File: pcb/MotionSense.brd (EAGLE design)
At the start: 59.4 x 59.2 mm, 18 parts

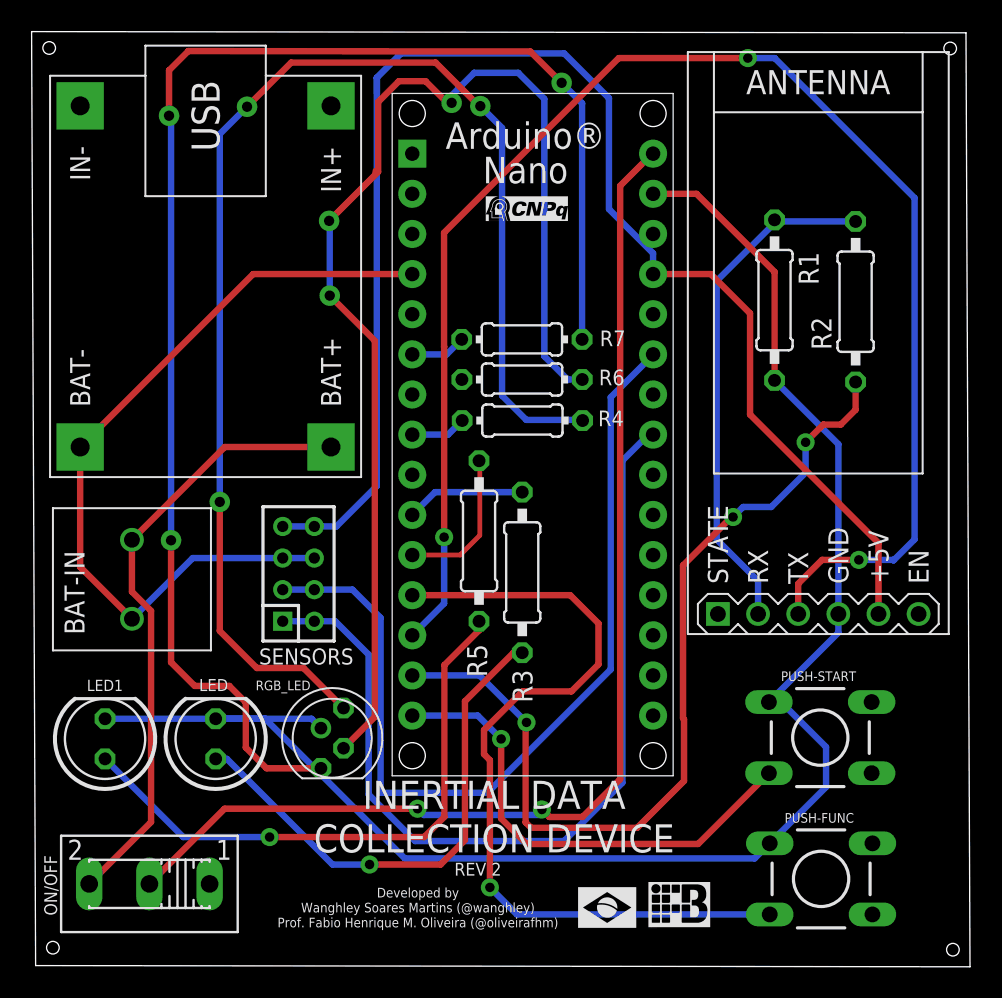
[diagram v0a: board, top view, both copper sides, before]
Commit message: [UPDATE] Wrong ports and errors in design fixing
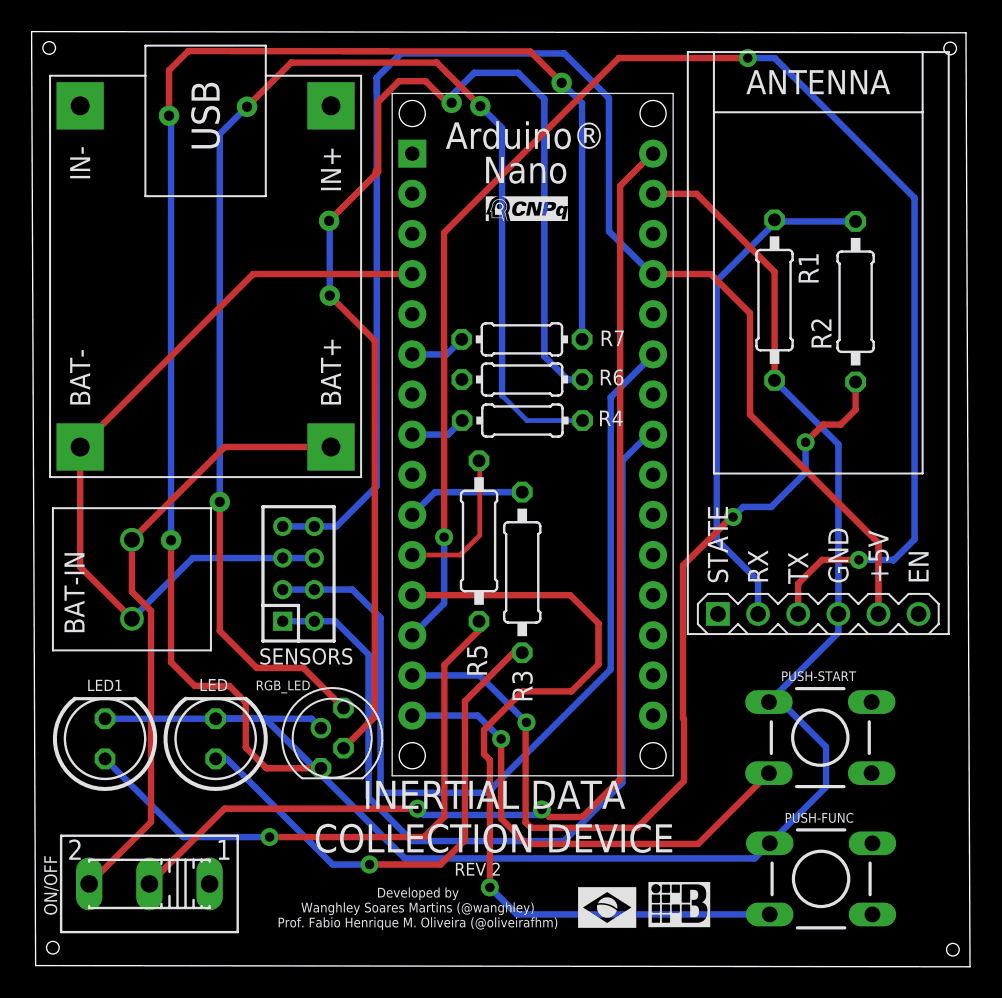
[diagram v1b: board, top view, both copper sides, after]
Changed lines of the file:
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@@
 <wire x1="40.5732" y1="36.9288" x2="41.9001" y2="36.9288" width="0.4064" layer="16"/>
 <wire x1="41.9001" y1="36.9288" x2="44.015659375" y2="34.813240625" width="0.4064" layer="16"/>
-<wire x1="44.015659375" y1="34.813240625" x2="44.015659375" y2="25.958796875" width="0.4064" layer="16"/>
-<wire x1="44.015659375" y1="25.958796875" x2="46.95570625" y2="23.01875" width="0.4064" layer="16"/>
-<wire x1="46.95570625" y1="23.01875" x2="56.379109375" y2="23.01875" width="0.4064" layer="16"/>
+<wire x1="44.015659375" y1="34.813240625" x2="44.015659375" y2="25.765759375" width="0.4064" layer="16"/>
+<wire x1="44.015659375" y1="25.765759375" x2="46.76266875" y2="23.01875" width="0.4064" layer="16"/>
+<wire x1="46.76266875" y1="23.01875" x2="56.379109375" y2="23.01875" width="0.4064" layer="16"/>
 <wire x1="61.716921875" y1="48.7400625" x2="60.0684625" y2="47.091603125" width="0.4064" layer="16"/>
 <wire x1="61.716921875" y1="48.7400625" x2="62.0115625" y2="48.7400625" width="0.4064" layer="16"/>
@@
 <wire x1="46.07051875" y1="72.86751875" x2="56.38038125" y2="72.86751875" width="0.4064" layer="16"/>
 <wire x1="56.38038125" y1="72.86751875" x2="59.2201" y2="70.0278" width="0.4064" layer="16"/>
-<wire x1="59.2201" y1="70.0278" x2="59.2201" y2="63.00588125" width="0.4064" layer="16"/>
-<wire x1="62.0115625" y1="58.9000625" x2="62.0115625" y2="60.21441875" width="0.4064" layer="16"/>
-<wire x1="62.0115625" y1="60.21441875" x2="59.2201" y2="63.00588125" width="0.4064" layer="16"/>
+<wire x1="59.2201" y1="70.0278" x2="59.2201" y2="61.603803125" width="0.4064" layer="16"/>
+<wire x1="62.0115625" y1="58.9000625" x2="61.923840625" y2="58.9000625" width="0.4064" layer="16"/>
+<wire x1="61.923840625" y1="58.9000625" x2="59.2201" y2="61.603803125" width="0.4064" layer="16"/>
 <wire x1="38.5732" y1="42.9288" x2="40.5732" y2="42.9288" width="0.4064" layer="16"/>
 <wire x1="76.2762" y1="37.3888" x2="76.2762" y2="41.8846" width="0.4064" layer="1"/>
@@
 <wire x1="57.4929" y1="49.8221" x2="57.4929" y2="49.819559375" width="0.4064" layer="16"/>
 <wire x1="36.316921875" y1="69.489321875" x2="39.11091875" y2="72.28331875" width="0.4064" layer="1"/>
-<wire x1="39.11091875" y1="72.28331875" x2="48.249840625" y2="72.28331875" width="0.4064" layer="1"/>
-<wire x1="48.249840625" y1="72.28331875" x2="50.8609625" y2="69.672196875" width="0.4064" layer="1"/>
-<wire x1="50.9371625" y1="69.672196875" x2="50.8609625" y2="69.672196875" width="0.4064" layer="1"/>
-<wire x1="50.9371625" y1="69.672196875" x2="51.0794" y2="69.529959375" width="0.4064" layer="1"/>
+<wire x1="39.11091875" y1="72.28331875" x2="48.326040625" y2="72.28331875" width="0.4064" layer="1"/>
+<wire x1="48.326040625" y1="72.28331875" x2="51.0794" y2="69.529959375" width="0.4064" layer="1"/>
 <via x="51.0794" y="69.529959375" extent="1-16" drill="0.65" diameter="1.3"/>
 <wire x1="51.0794" y1="69.529959375" x2="52.45608125" y2="68.153278125" width="0.4064" layer="16"/>
-<wire x1="52.45608125" y1="68.153278125" x2="52.45608125" y2="51.206403125" width="0.4064" layer="16"/>
-<wire x1="52.45608125" y1="51.206403125" x2="53.99024375" y2="49.672240625" width="0.4064" layer="16"/>
+<wire x1="52.45608125" y1="51.206403125" x2="52.45608125" y2="68.153278125" width="0.4064" layer="16"/>
 <wire x1="57.51068125" y1="49.672240625" x2="57.551321875" y2="49.6316" width="0.4064" layer="16"/>
-<wire x1="57.51068125" y1="49.672240625" x2="53.99024375" y2="49.672240625" width="0.4064" layer="16"/>
-<wire x1="53.99024375" y1="49.672240625" x2="57.4929" y2="49.8221" width="0" layer="19" extent="16-16"/>
+<wire x1="57.551321875" y1="49.6316" x2="54.030884375" y2="49.6316" width="0.3048" layer="16"/>
+<wire x1="54.030884375" y1="49.6316" x2="52.45608125" y2="51.206403125" width="0.3048" layer="16"/>
+<wire x1="57.51068125" y1="49.672240625" x2="57.4929" y2="49.8221" width="0" layer="19" extent="16-16"/>
 </signal>
 <signal name="N$18">

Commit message: [UPDATE] Fixing airwire, dimesion, drill distance & overlap errors in electronic design
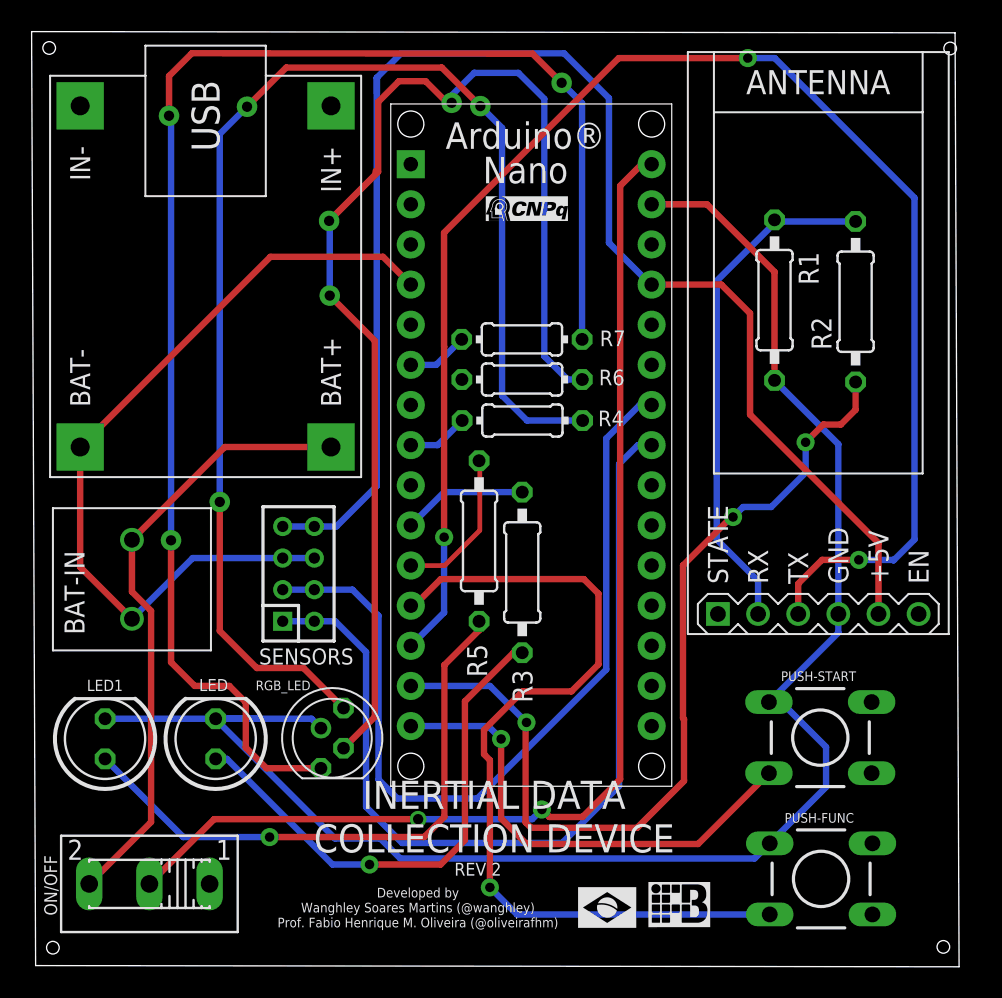
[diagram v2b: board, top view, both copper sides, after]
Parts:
- moved ARDUINO-NANO 0.67 mm to (54.3, 48.1)
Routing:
- net N$7: track 56.9 -> 53.8 mm
- net N$4: track 105.8 -> 108.5 mm
- net N$12: track 52.6 -> 54.9 mm
- net NEGATIVE: track 50.9 -> 52.0 mm
- net N$5: track 96.5 -> 97.2 mm
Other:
- board size 59.4 x 59.2 mm -> 58.7 x 59.2 mm

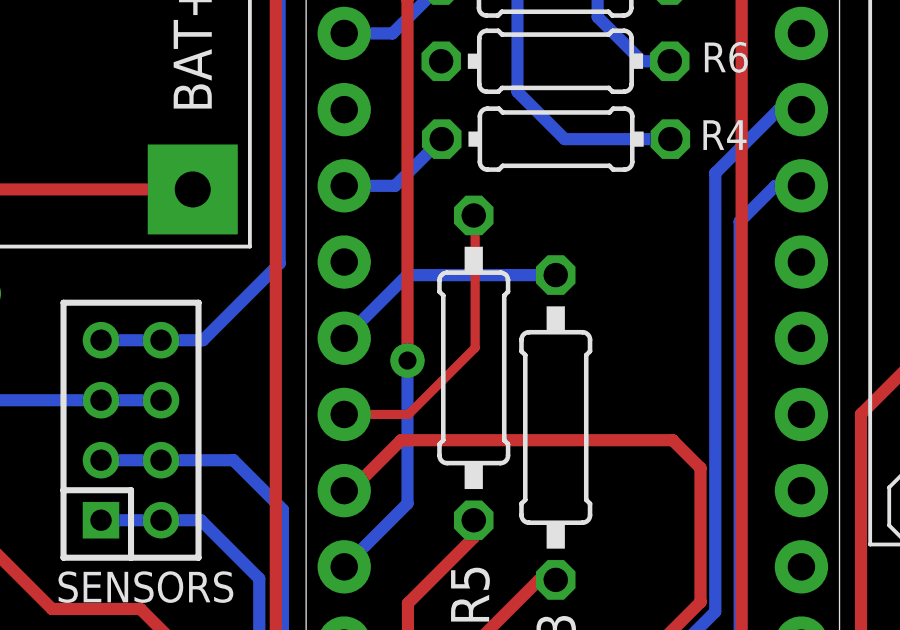
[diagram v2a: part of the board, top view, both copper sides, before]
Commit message: [UPDATE] connecting new wires to LEDs after schematic error correction
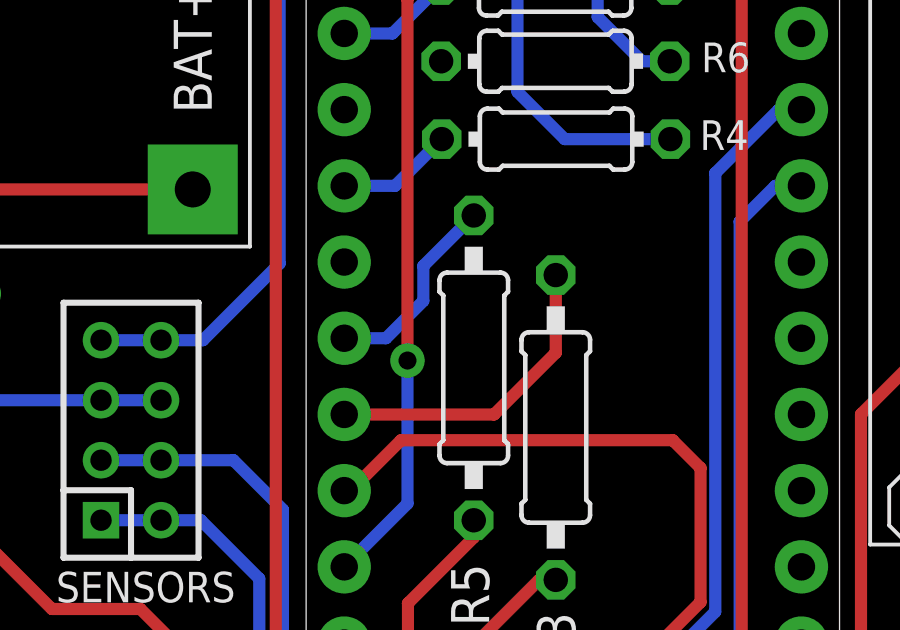
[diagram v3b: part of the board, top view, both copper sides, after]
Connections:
- net N$13: now also R3.2; no longer R5.2
- net N$9: now also R5.2; no longer R3.2
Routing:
- net N$9: track 7.96 -> 6.70 mm
- net N$13: track 9.71 -> 10.5 mm
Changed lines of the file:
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@@
 <wire x1="59.860184375" y1="26.499825" x2="59.860184375" y2="46.883325" width="0.4064" layer="16"/>
-</signal>
-<signal name="N$9">
-<contactref element="R3" pad="2"/>
-<contactref element="ARDUINO-NANO" pad="J1.10"/>
-<wire x1="53.708296875" y1="45.1231" x2="53.731159375" y2="45.1002375" width="0.4064" layer="16"/>
-<wire x1="53.731159375" y1="45.1002375" x2="48.785778125" y2="45.1002375" width="0.4064" layer="16"/>
-<wire x1="48.785778125" y1="45.1002375" x2="46.680121875" y2="42.99458125" width="0.4064" layer="16"/>
 </signal>
 <signal name="N$10">
@@
 <wire x1="57.52084375" y1="69.70775625" x2="57.52084375" y2="54.767478125" width="0.4064" layer="16"/>
 </signal>
-<signal name="N$13">
-<contactref element="R5" pad="2"/>
-<contactref element="ARDUINO-NANO" pad="J1.11"/>
-<wire x1="46.680121875" y1="40.45458125" x2="48.821340625" y2="40.45458125" width="0.3048" layer="1"/>
-<wire x1="48.821340625" y1="40.45458125" x2="51.043840625" y2="42.67708125" width="0.3048" layer="1"/>
-<wire x1="51.043840625" y1="42.67708125" x2="51.043840625" y2="47.040796875" width="0.3048" layer="1"/>
-<wire x1="51.043840625" y1="47.040796875" x2="50.99811875" y2="47.08651875" width="0.3048" layer="1"/>
-</signal>
 <signal name="N$21">
 <contactref element="R6" pad="1"/>
 </signal>
+<signal name="N$9">
+<contactref element="ARDUINO-NANO" pad="J1.10"/>
+<contactref element="R5" pad="2"/>
+<wire x1="50.99811875" y1="47.08651875" x2="49.316640625" y2="45.405040625" width="0.4064" layer="16"/>
+<wire x1="49.316640625" y1="45.405040625" x2="49.316640625" y2="44.238440625" width="0.4064" layer="16"/>
+<wire x1="49.316640625" y1="44.238440625" x2="48.07278125" y2="42.99458125" width="0.4064" layer="16"/>
+<wire x1="48.07278125" y1="42.99458125" x2="46.680121875" y2="42.99458125" width="0.4064" layer="16"/>
+</signal>
+<signal name="N$13">
+<contactref element="ARDUINO-NANO" pad="J1.11"/>
+<contactref element="R3" pad="2"/>
+<wire x1="53.731159375" y1="45.1002375" x2="53.731159375" y2="42.509440625" width="0.4064" layer="1"/>
+<wire x1="53.731159375" y1="42.509440625" x2="51.673759375" y2="40.452040625" width="0.4064" layer="1"/>
+<wire x1="51.673759375" y1="40.452040625" x2="46.6826625" y2="40.452040625" width="0.4064" layer="1"/>
+<wire x1="46.6826625" y1="40.452040625" x2="46.680121875" y2="40.45458125" width="0.4064" layer="1"/>
+</signal>
 </signals>
